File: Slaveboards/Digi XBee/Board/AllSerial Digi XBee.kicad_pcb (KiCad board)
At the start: 2 copper layers, 67.4 x 44.8 mm, 2 parts, among them X1 AllSerial Slaveboard

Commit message: Added new boards
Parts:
- moved JP1 15.9 mm to (173.0, 111.6)

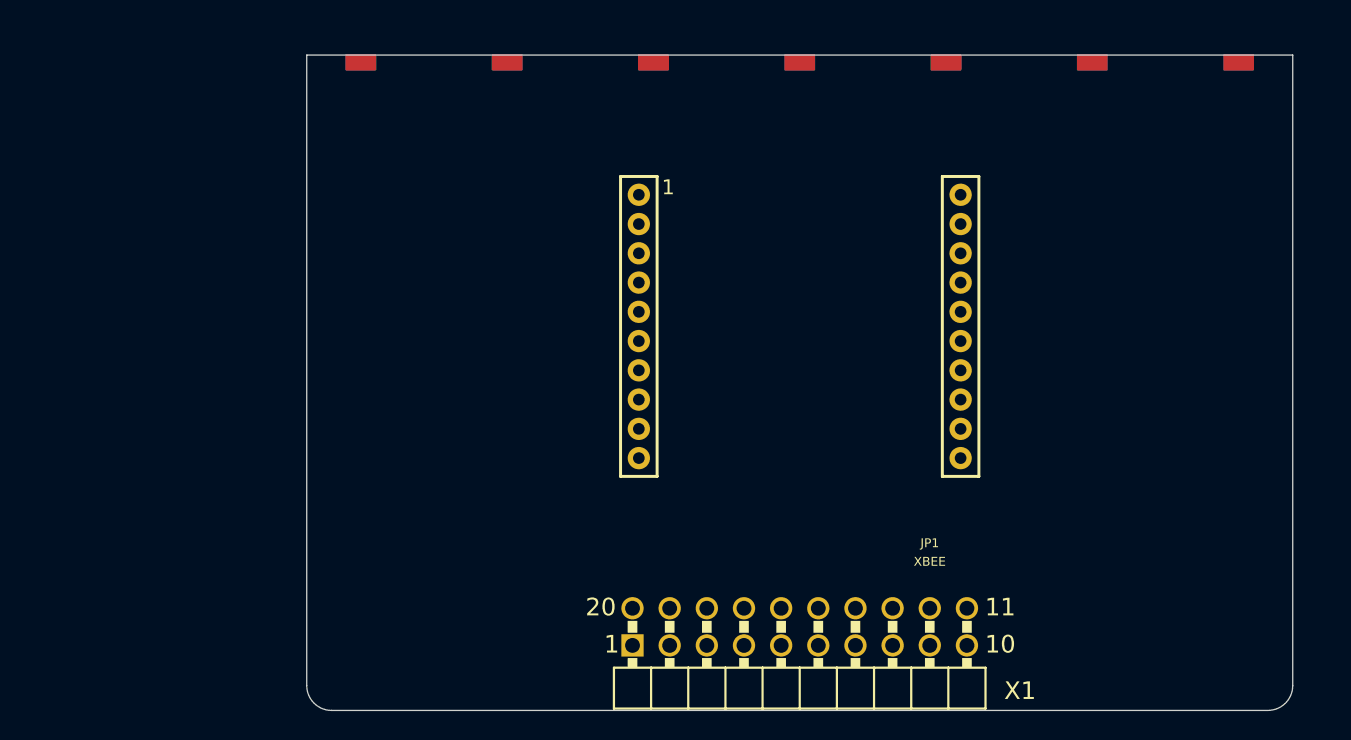
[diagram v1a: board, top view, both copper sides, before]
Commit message: Migrate to KiCad 9
Add eBus board
Add various libraries
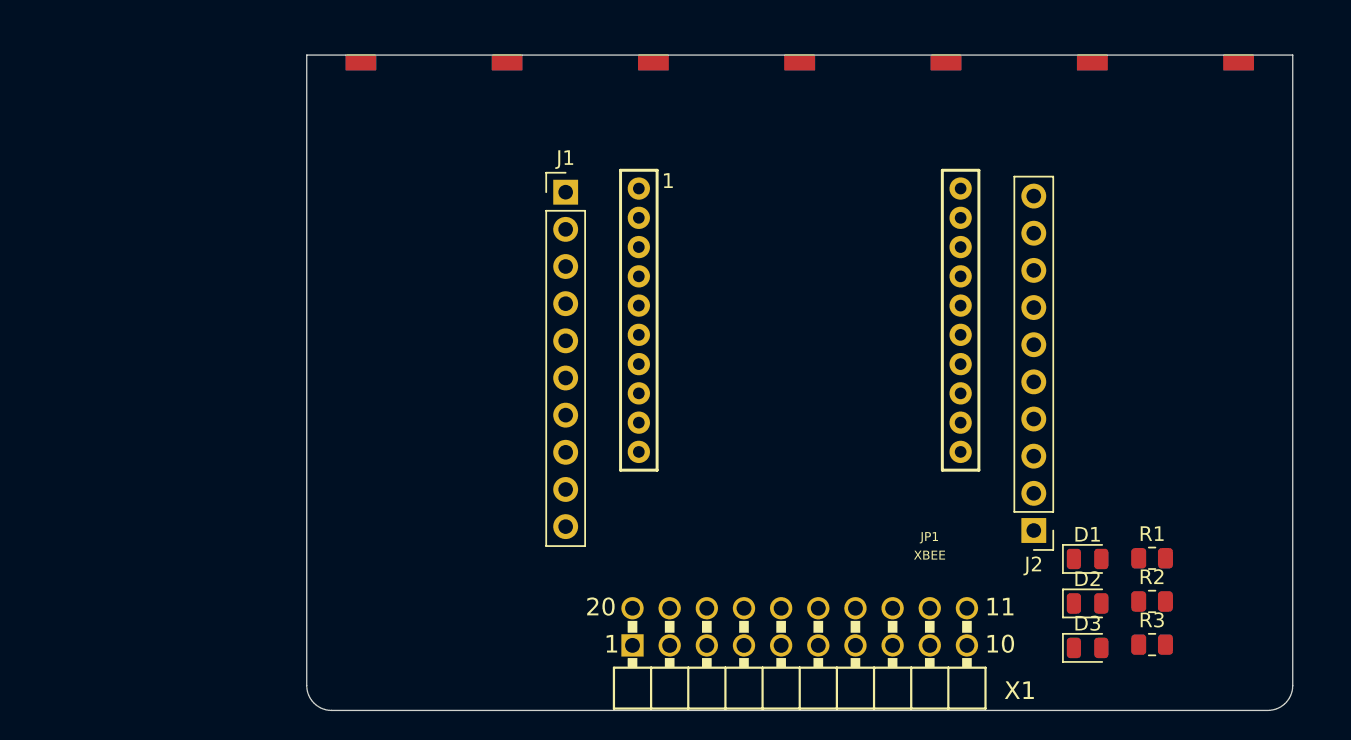
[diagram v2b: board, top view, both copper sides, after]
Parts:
- added D1: LED, LED_SMD:LED_0805_2012Metric, F.Cu at (192.7, 116.5)
- added D2: LED, LED_SMD:LED_0805_2012Metric, F.Cu at (192.7, 119.6)
- added D3: LED, LED_SMD:LED_0805_2012Metric, F.Cu at (192.7, 122.6)
- added J1: Conn_01x10, Connector_PinHeader_2.54mm:PinHeader_1x10_P2.54mm_Vertical, F.Cu at (157.0, 91.4)
- added J2: Conn_01x10, Connector_PinHeader_2.54mm:PinHeader_1x10_P2.54mm_Vertical, F.Cu at (189.0, 114.6)
- added R1: 1k, Resistor_SMD:R_0805_2012Metric, F.Cu at (197.1, 116.5)
- added R2: 1k, Resistor_SMD:R_0805_2012Metric, F.Cu at (197.1, 119.4)
- added R3: 1k, Resistor_SMD:R_0805_2012Metric, F.Cu at (197.1, 122.4)
- moved JP1 0.42 mm to (173.0, 111.2)
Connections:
- JP1 pad 11: unconnected-(JP1-DIO4-Pad11) -> Net-(J2-Pin_1)
- JP1 pad 13: unconnected-(JP1-DIO9-Pad13) -> /DIO9
- JP1 pad 14: unconnected-(JP1-RES-Pad14) -> Net-(J2-Pin_4)
- JP1 pad 15: unconnected-(JP1-DIO5-Pad15) -> /DIO5
- JP1 pad 17: unconnected-(JP1-DIO3-Pad17) -> Net-(J2-Pin_7)
- JP1 pad 18: unconnected-(JP1-DIO2-Pad18) -> Net-(J2-Pin_8)
- JP1 pad 19: unconnected-(JP1-DIO1-Pad19) -> Net-(J2-Pin_9)
- JP1 pad 20: unconnected-(JP1-DIO0-Pad20) -> Net-(J2-Pin_10)
- JP1 pad 4: unconnected-(JP1-DIO12-Pad4) -> Net-(J1-Pin_4)
- JP1 pad 5: unconnected-(JP1-RESET-Pad5) -> Net-(J1-Pin_5)
- JP1 pad 6: unconnected-(JP1-RSSI-Pad6) -> /RSSI
- JP1 pad 7: unconnected-(JP1-DIO11-Pad7) -> Net-(J1-Pin_7)
- JP1 pad 8: unconnected-(JP1-RES-Pad8) -> Net-(J1-Pin_8)
- X1 pad 13: unconnected-(X1A-DTR-Pad13) -> /DTR

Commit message: improve AllSerial library
add assets for README
update README
cleanup
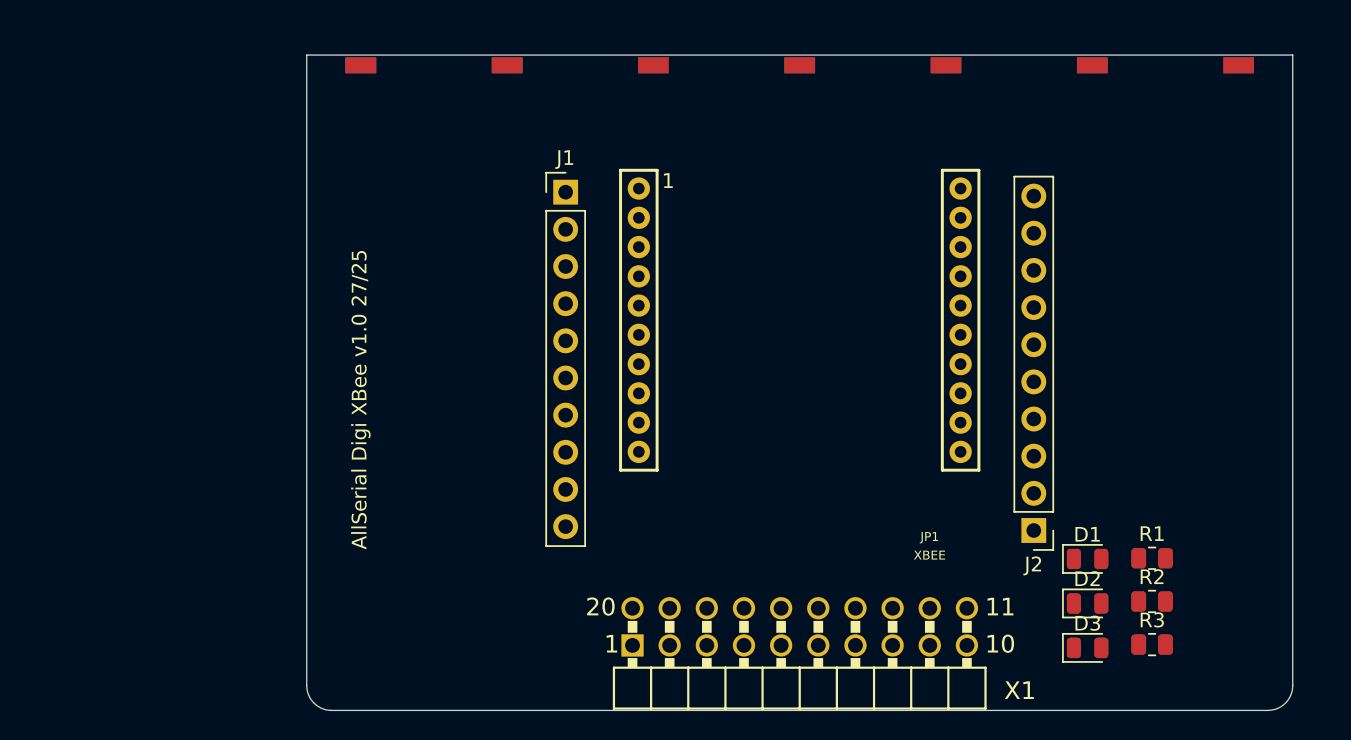
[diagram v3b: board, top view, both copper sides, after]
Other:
- board text added: "AllSerial Digi XBee v1.0 27/25"

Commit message: Improve libraries
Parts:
- added D4: GN, LED_SMD:LED_0805_2012Metric, F.Cu at (122.1, 99.0)
- added J3: Conn_01x02, AllSerial:Metz_PT11302HBBN_182, F.Cu at (197.0, 90.0)
- added R4: 220, Resistor_SMD:R_0805_2012Metric, F.Cu at (132.9, 88.6)
- added R5: 1k, Resistor_SMD:R_0805_2012Metric, F.Cu at (132.9, 91.6)
- added S1: 31-XX, Button_Switch_SMD:SW_SPST_CK_RS282G05A3, F.Cu at (152.0, 89.1)
- added S2: 31-XX, Button_Switch_SMD:SW_SPST_CK_RS282G05A3, F.Cu at (151.4, 97.4)
- added S3: 31-XX, Button_Switch_SMD:SW_SPST_CK_RS282G05A3, F.Cu at (151.4, 111.2)
- D1: value LED -> YL
- D2: value LED -> RD
- D3: value LED -> GN
- moved R2 46.7 mm to (152.9, 104.2), turned to 180 degrees
- moved D2 46.6 mm to (148.7, 104.2)
- moved R1 22.5 mm to (178.3, 104.2)
- moved D3 19.7 mm to (178.3, 109.1), turned to 180 degrees
- moved R3 19.7 mm to (182.6, 109.1)
- moved D1 15.9 mm to (182.7, 104.2), turned to 180 degrees
- moved J2 8.82 mm to (197.0, 118.3)
- moved J1 7.35 mm to (164.1, 93.3)
- moved JP1 7.00 mm to (180.0, 111.2)
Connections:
- net Net-(J1-Pin_7) renamed /RST
- net Net-(J2-Pin_10) renamed /DIO0
- net VCC renamed +3.3V
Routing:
- net +3.3V: track 0.00 -> 3.59 mm
- added copper zone on B.Cu, net GND
- added copper zone on F.Cu, net GND
